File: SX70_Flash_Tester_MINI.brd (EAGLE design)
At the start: 33 x 35.5 mm, 16 parts

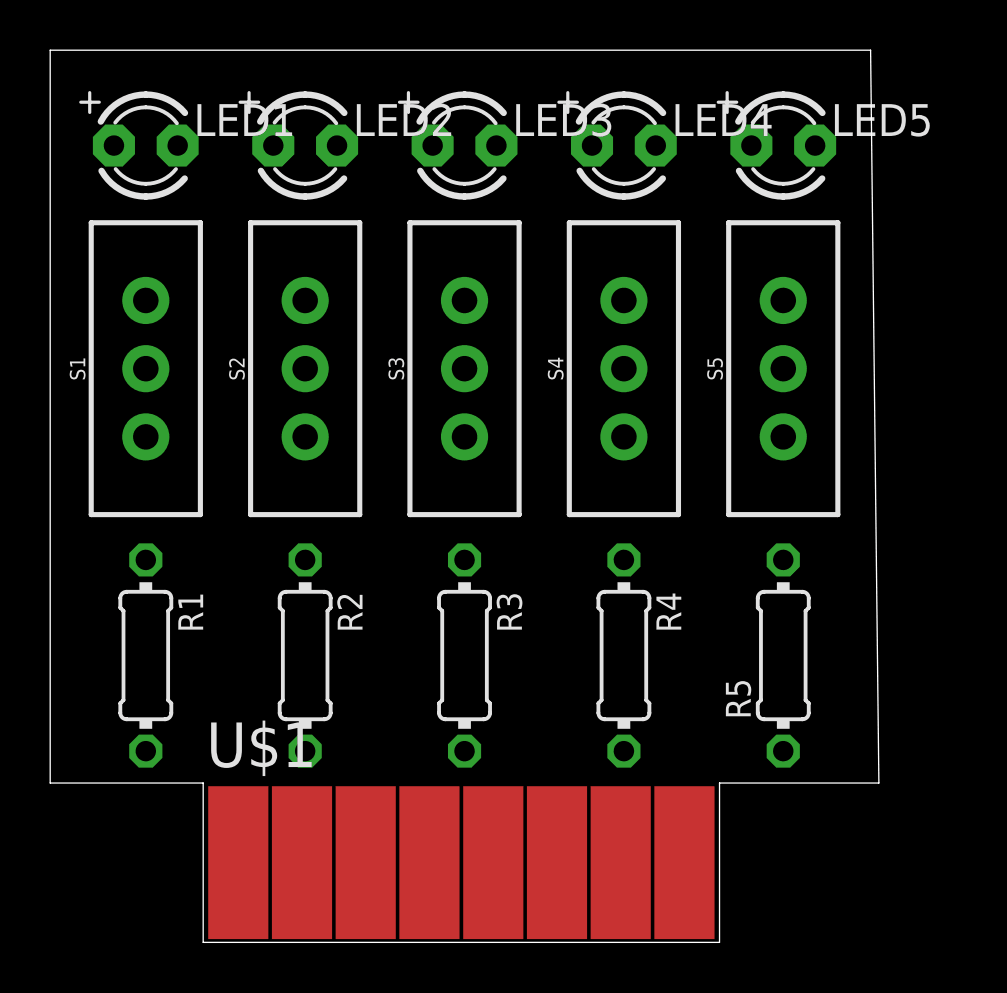
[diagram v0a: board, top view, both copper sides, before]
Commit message: I have designed and ordered at OSHPARK a "mini" flash tester.
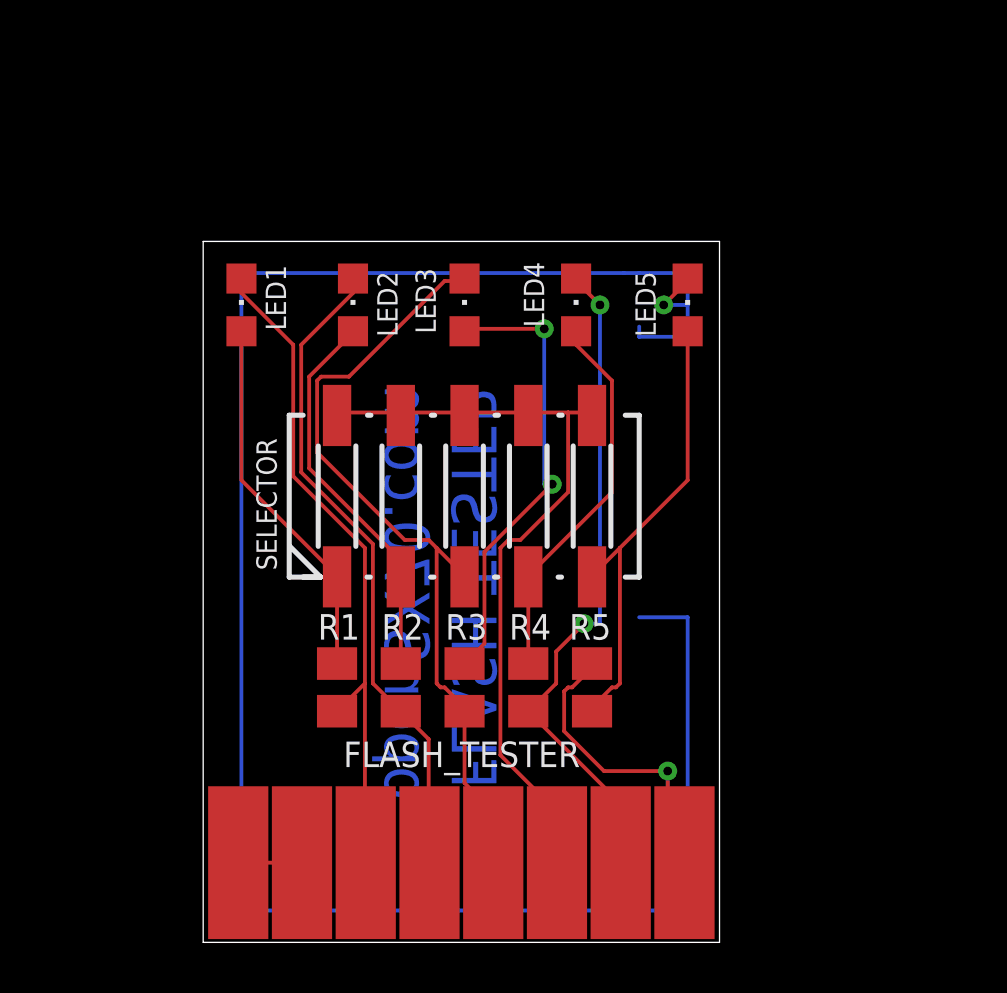
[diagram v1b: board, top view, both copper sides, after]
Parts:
- removed S1, S2, S3, S4, S5: (no value), SparkFun-Switches:SWITCH_SPDT_PTH_11.6X4.0MM_LOCK
- added SELECTOR: 219-05J, switch-dil:CTS-219-05J
- LED1, LED2, LED3, LED4, LED5: device adafruit:LED3MM -> led:CHIPLED_0805
- R1, R2, R3, R4, R5: device rcl:0204/7 -> rcl:M0805
- moved R5 7.73 mm to (21.6, 10.2)
- moved R1 7.73 mm to (11.4, 10.2)
- moved LED5 7.41 mm to (25.4, 25.4)
- moved LED1 7.41 mm to (7.62, 25.4)
- moved LED4 6.63 mm to (21.0, 25.4)
- moved LED2 6.63 mm to (12.1, 25.4)
- moved LED3 6.35 mm to (16.5, 25.4)
- moved R2 4.02 mm to (14.0, 10.2)
- moved R4 4.02 mm to (19.1, 10.2)
- moved R3 1.27 mm to (16.5, 10.2)
- renumbered U$1 to FLASH_TESTER
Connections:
- removed net N$12: FLASH_TESTER.VCC-6V, S1.2, S2.2, S3.2, S4.2, S5.2
- new net N$4: FLASH_TESTER.VCC-6V, SELECTOR.10, SELECTOR.6, SELECTOR.7, SELECTOR.8, SELECTOR.9
- net N$1: now also SELECTOR.1; no longer S1.3
- net N$10: now also LED1.C; no longer LED1.K
- net N$14: now also SELECTOR.4; no longer S4.3
- net N$2: now also SELECTOR.2; no longer S2.3
- net N$5: now also SELECTOR.5; no longer S5.3
- net N$6: now also LED5.C; no longer LED5.K
- net N$7: now also LED4.C; no longer LED4.K
- net N$8: now also LED3.C, SELECTOR.3; no longer LED3.K, S3.3
- net N$9: now also LED2.C; no longer LED2.K
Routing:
- net N$6: track 0.00 -> 99.4 mm, vias 0 -> 2
- net N$8: track 0.00 -> 32.0 mm
- net N$4: track 0.00 -> 31.0 mm
- net N$10: track 0.00 -> 26.9 mm
- net N$7: track 0.00 -> 26.7 mm, vias 0 -> 2
- net N$9: track 0.00 -> 26.2 mm
- net N$5: track 0.00 -> 18.4 mm
- net N$3: track 0.00 -> 18.4 mm, vias 0 -> 2
- net N$2: track 0.00 -> 15.5 mm
- net N$14: track 0.00 -> 15.2 mm
- net N$1: track 0.00 -> 14.8 mm
- net N$11: track 0.00 -> 2.54 mm
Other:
- board size 33 x 35.5 mm -> 20.6 x 27.9 mm
- board text added: "FLASH TESTER openSX70.com"
